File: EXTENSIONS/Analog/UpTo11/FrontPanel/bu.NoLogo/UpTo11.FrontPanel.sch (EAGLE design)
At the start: 2 parts

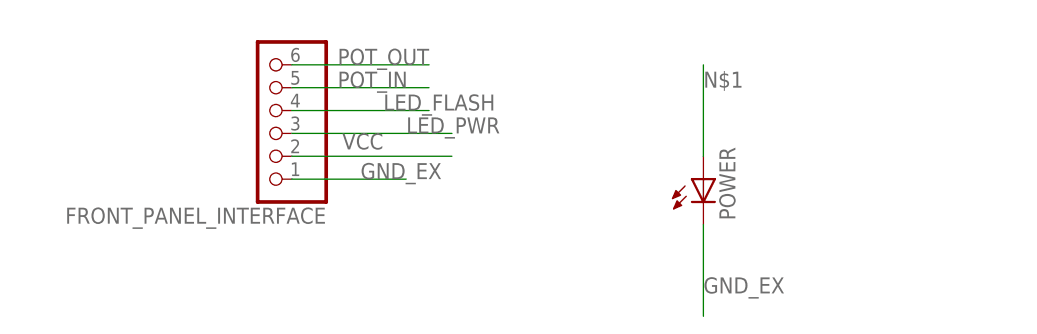
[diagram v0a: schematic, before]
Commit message: Create UpTo11 Front Panel
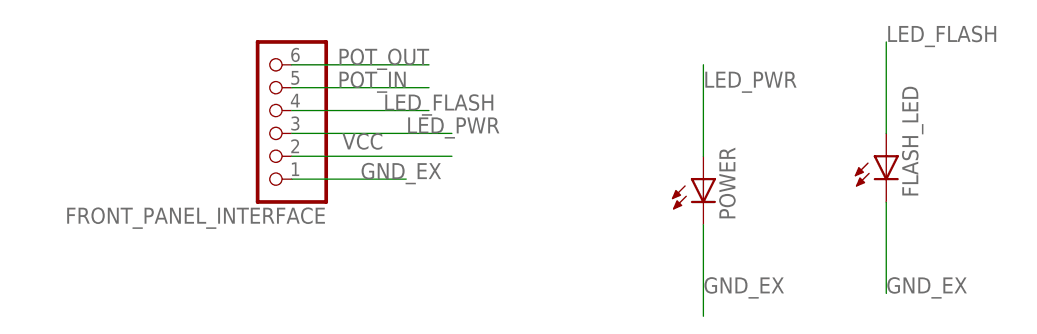
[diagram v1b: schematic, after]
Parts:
- added FLASH_LED: (no value), adafruit:LED5MM
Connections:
- removed net N$1: POWER.A
- net GND_EX: now also FLASH_LED.C
- net LED_FLASH: now also FLASH_LED.A
- net LED_PWR: now also POWER.A
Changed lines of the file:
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@@
 <classes>
 <class number="0" name="default" width="0" drill="0">
+<clearance class="0" value="0.205"/>
 </class>
 </classes>
@@
 <part name="FRONT_PANEL_INTERFACE" library="adafruit" deviceset="PINHD-1X6" device=""/>
 <part name="POWER" library="adafruit" deviceset="LED" device="SMT1206"/>
+<part name="FLASH_LED" library="adafruit" deviceset="LED" device="5MM"/>
 </parts>
 <sheets>
@@
 <instance part="FRONT_PANEL_INTERFACE" gate="A" x="-2.54" y="81.28" rot="R180"/>
 <instance part="POWER" gate="G$1" x="45.72" y="73.66"/>
+<instance part="FLASH_LED" gate="G$1" x="66.04" y="76.2"/>
 </instances>
 <busses>
@@
 <wire x1="0" y1="81.28" x2="15.24" y2="81.28" width="0.1524" layer="91"/>
 <label x="10.16" y="81.28" size="1.778" layer="95"/>
+</segment>
+<segment>
+<pinref part="FLASH_LED" gate="G$1" pin="A"/>
+<wire x1="66.04" y1="78.74" x2="66.04" y2="88.9" width="0.1524" layer="91"/>
+<label x="66.04" y="88.9" size="1.778" layer="95"/>
 </segment>
 </net>
@@
 <wire x1="45.72" y1="68.58" x2="45.72" y2="58.42" width="0.1524" layer="91"/>
 <label x="45.72" y="60.96" size="1.778" layer="95"/>
+</segment>
+<segment>
+<pinref part="FLASH_LED" gate="G$1" pin="C"/>
+<wire x1="66.04" y1="71.12" x2="66.04" y2="60.96" width="0.1524" layer="91"/>
+<label x="66.04" y="60.96" size="1.778" layer="95"/>
 </segment>
 </net>
@@
 <wire x1="0" y1="78.74" x2="17.78" y2="78.74" width="0.1524" layer="91"/>
 <label x="12.7" y="78.74" size="1.778" layer="95"/>
+</segment>
+<segment>
+<pinref part="POWER" gate="G$1" pin="A"/>
+<wire x1="45.72" y1="76.2" x2="45.72" y2="86.36" width="0.1524" layer="91"/>
+<label x="45.72" y="83.82" size="1.778" layer="95"/>
 </segment>
 </net>
@@
 </segment>
 </net>
-<net name="N$1" class="0">
-<segment>
-<pinref part="POWER" gate="G$1" pin="A"/>
-<wire x1="45.72" y1="76.2" x2="45.72" y2="86.36" width="0.1524" layer="91"/>
-<label x="45.72" y="83.82" size="1.778" layer="95"/>
-</segment>
-</net>
